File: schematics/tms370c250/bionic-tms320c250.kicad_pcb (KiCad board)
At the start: 2 copper layers, 31.7 x 68.6 mm, 10 parts, among them J1 Bionic-P135, J2 Bionic-P245, U1 TMS370C250, U2 11AA010-I/TT

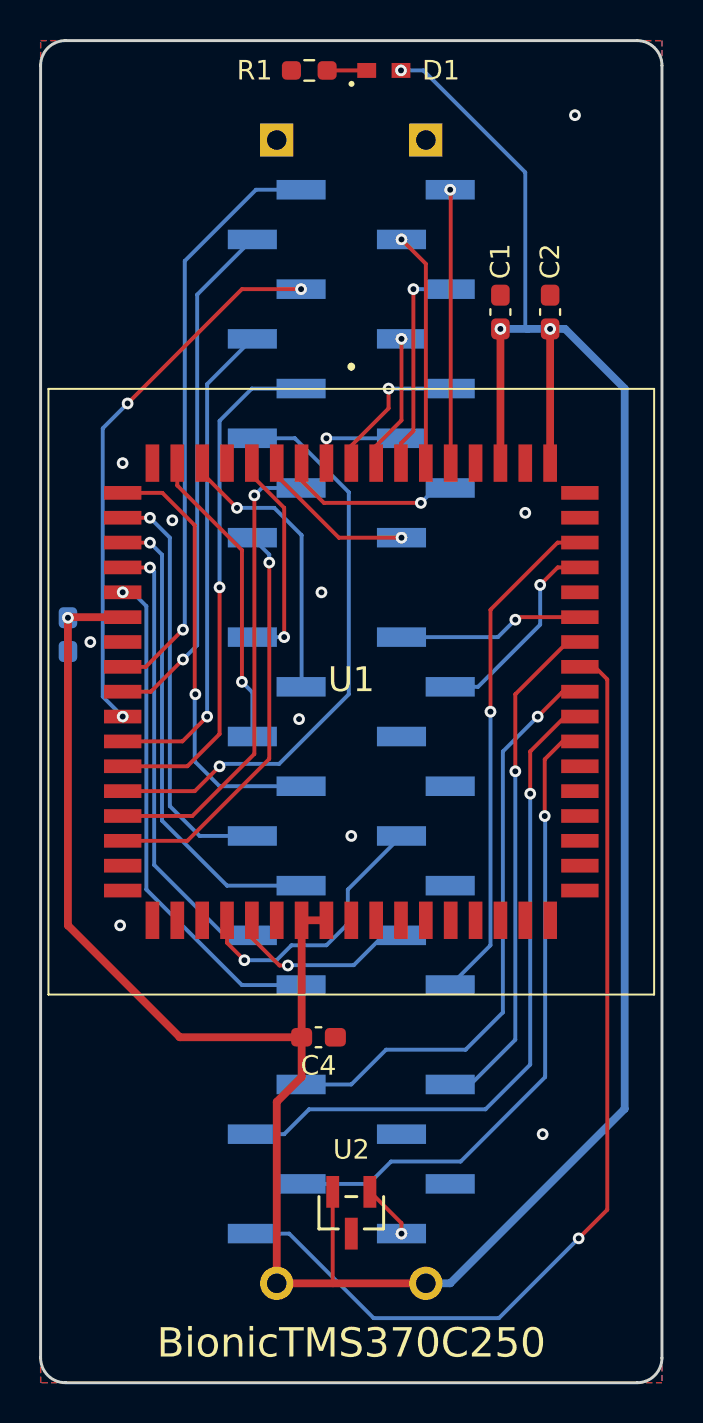
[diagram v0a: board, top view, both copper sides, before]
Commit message: [TMS320C250] Fix missing MC and OCF connection
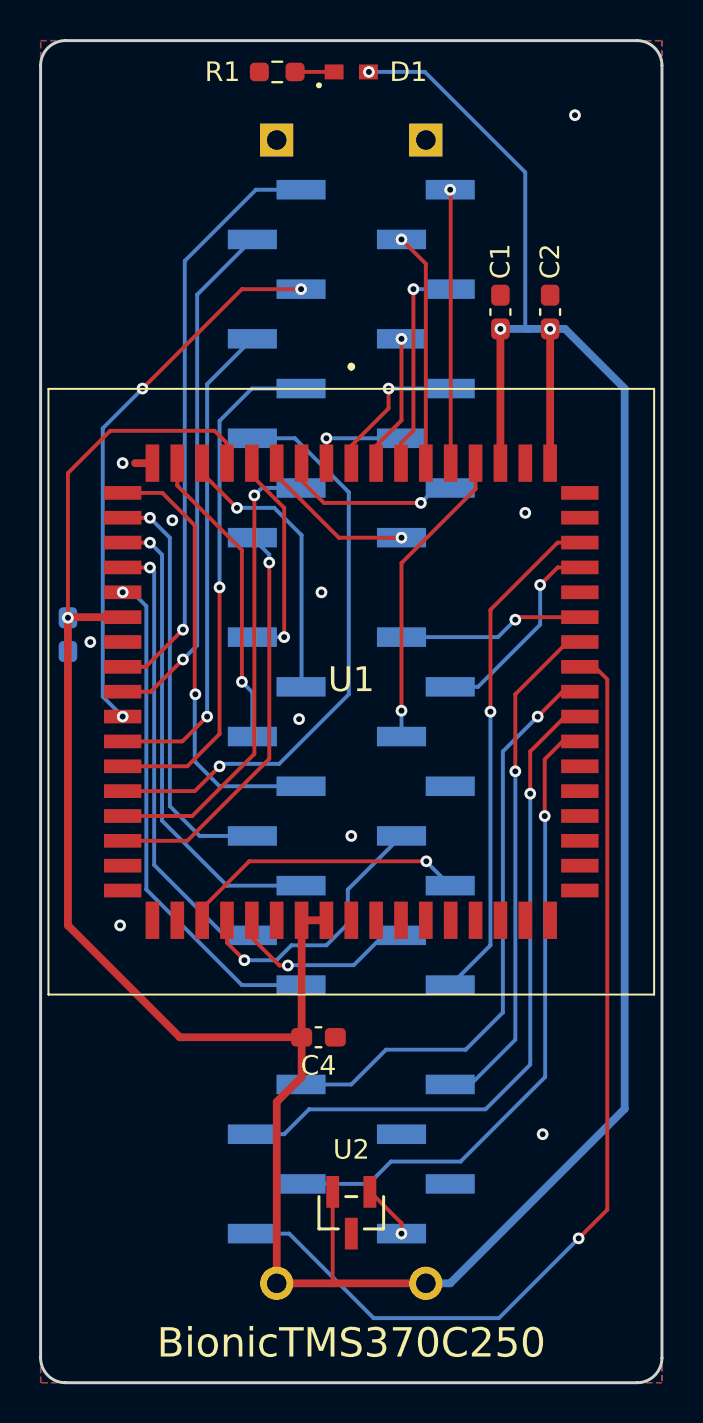
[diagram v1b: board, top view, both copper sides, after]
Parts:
- moved D1 1.67 mm to (113.7, 71.6)
- moved R1 1.64 mm to (109.9, 71.6)
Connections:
- J2 pad 33: unconnected-(J2-P45-Pad33) -> /P45
- J2 pad 35: /P43 -> unconnected-(J2-P43-Pad35)
- J2 pad 36: unconnected-(J2-P42-Pad36) -> /P42
- U1 pad 6: unconnected-(U1-MC-Pad6) -> VCC
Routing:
- net VCC: track 154.0 -> 173.3 mm
- net /P42: track 0.00 -> 15.5 mm, vias 0 -> 1
- net /P45: track 0.00 -> 14.8 mm, vias 0 -> 1
- net GND: track 0.00 -> 0.89 mm
